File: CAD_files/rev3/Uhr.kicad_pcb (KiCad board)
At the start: 2 copper layers, 28.5 x 31 mm, 37 parts, among them J2 Battery, J3 Conn_02x03_Odd_Even, J4 2171750001, U1 ATMEGA328P-AUR, U2 DS3231M_TRL, U3 BQ24075RGT, U4 TPS79333-EP, U5 DM-OLED096-636

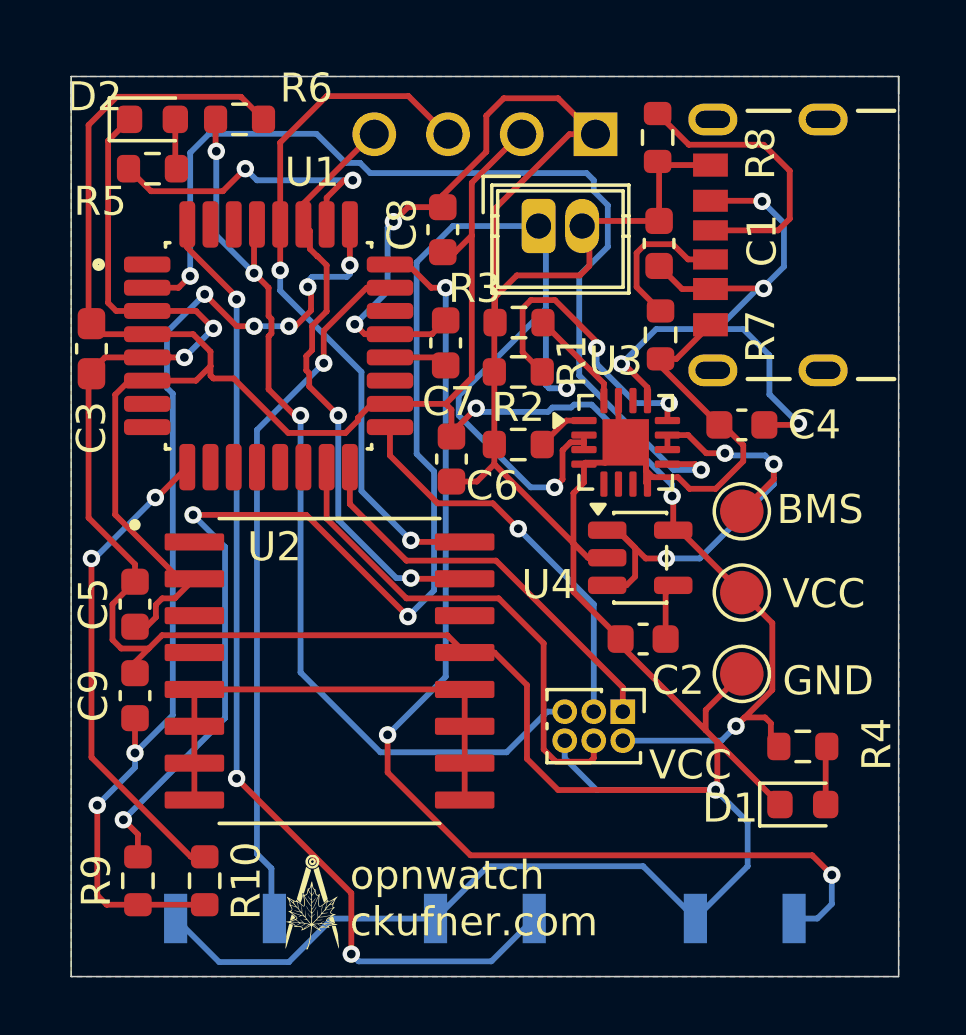
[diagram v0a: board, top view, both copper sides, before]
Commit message: removed leftover traces from rev2
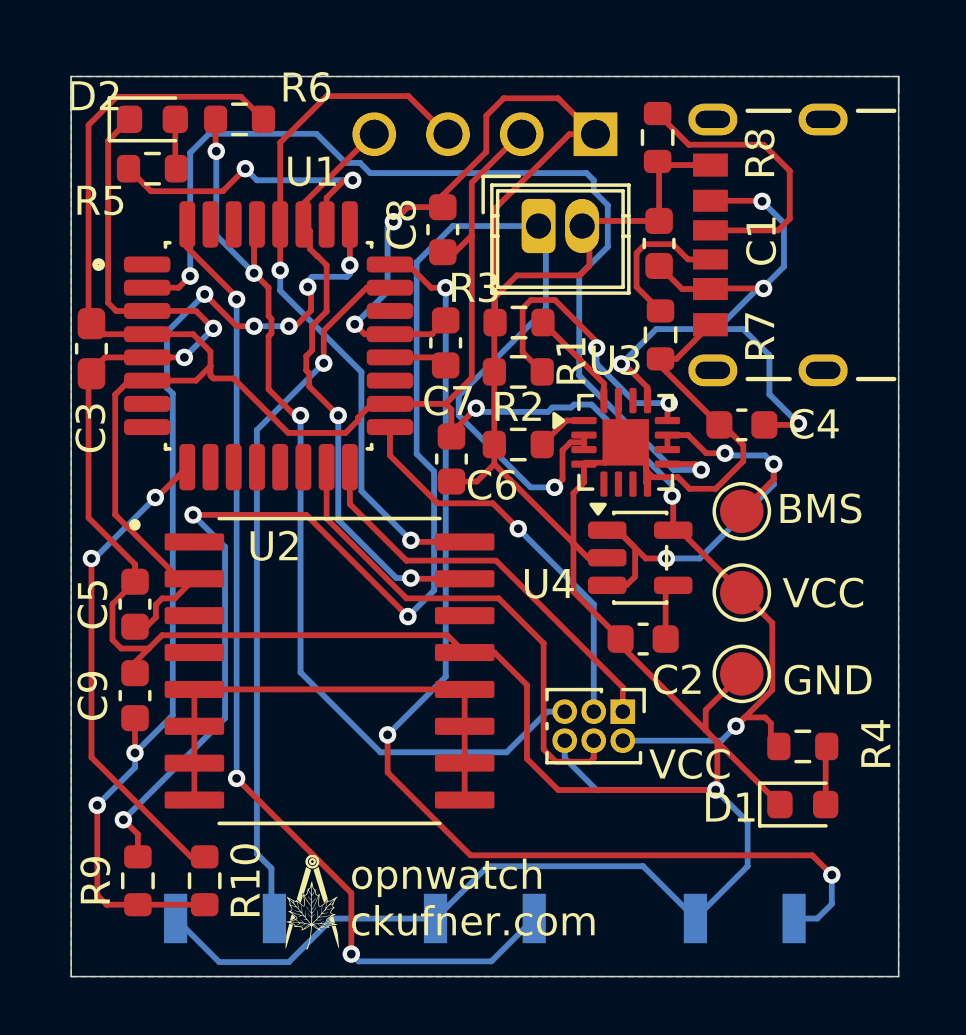
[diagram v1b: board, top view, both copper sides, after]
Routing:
- net BAT_POS: track 58.6 -> 55.2 mm, vias 5 -> 4
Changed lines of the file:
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@@
-	)
-	(via
-		(at 44.366853 25.738695)
-		(size 0.6)
-		(drill 0.3)
-		(layers "F.Cu" "B.Cu")
-		(capping no)
-		(covering
-			(front no)
-			(back no)
-		)
-		(plugging
-			(front no)
-			(back no)
-		)
-		(filling no)
-		(net "BAT_POS")
 	)
 	(via
@@
 	)
 	(segment
-		(start 43.65 25.625)
-		(end 43.65 23)
-		(width 0.2)
-		(layer "B.Cu")
-		(net "BAT_POS")
-	)
-	(segment
 		(start 39.8 28.6)
 		(end 39.2 28)
@@
 	)
 	(segment
-		(start 44.366853 25.738695)
-		(end 43.763695 25.738695)
-		(width 0.2)
-		(layer "B.Cu")
-		(net "BAT_POS")
-	)
-	(segment
 		(start 39.8 32.7)
 		(end 39.8 28.6)
@@
 		(start 43.95 29.15)
 		(end 43.126471 29.15)
-		(width 0.2)
-		(layer "B.Cu")
-		(net "BAT_POS")
-	)
-	(segment
-		(start 43.763695 25.738695)
-		(end 43.65 25.625)
 		(width 0.2)
 		(layer "B.Cu")
@@
 		(polygon
 			(pts
-				(xy 27.3 15) (xy 55.8 15) (xy 55.8 46) (xy 27.3 46)
+				(xy 55.8 46) (xy 55.8 15) (xy 27.3 15) (xy 27.3 46)
 			)
 		)
